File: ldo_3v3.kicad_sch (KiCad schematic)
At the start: 5 parts, among them U8 NCP1117-3.3

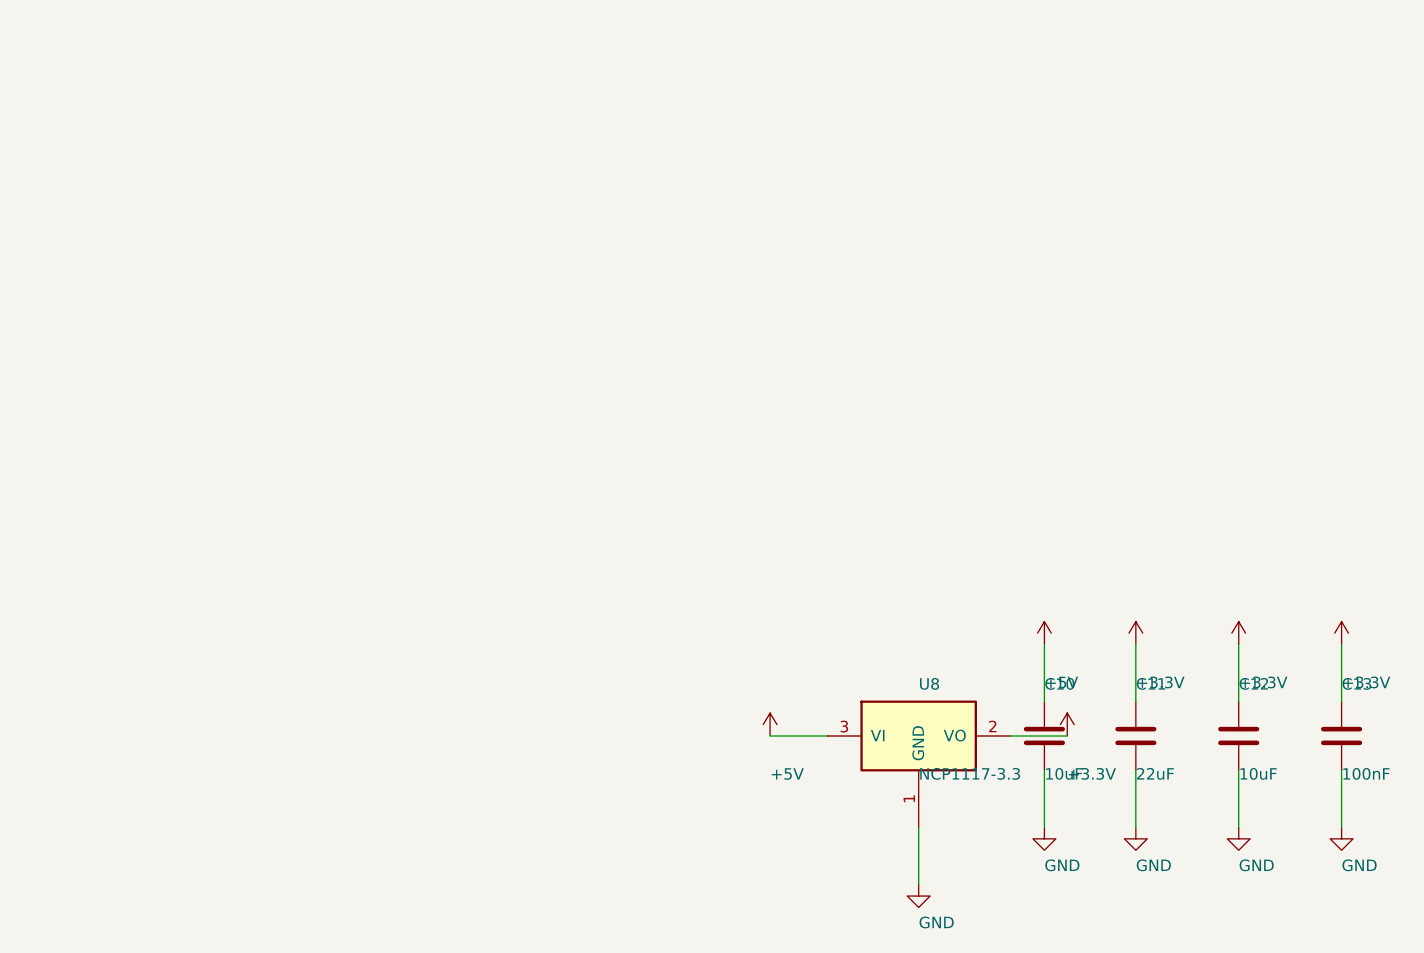
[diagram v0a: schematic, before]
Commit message: WIP: J18/Q2/Q3/R30/R31 + reguardado KiCad de todas las hojas
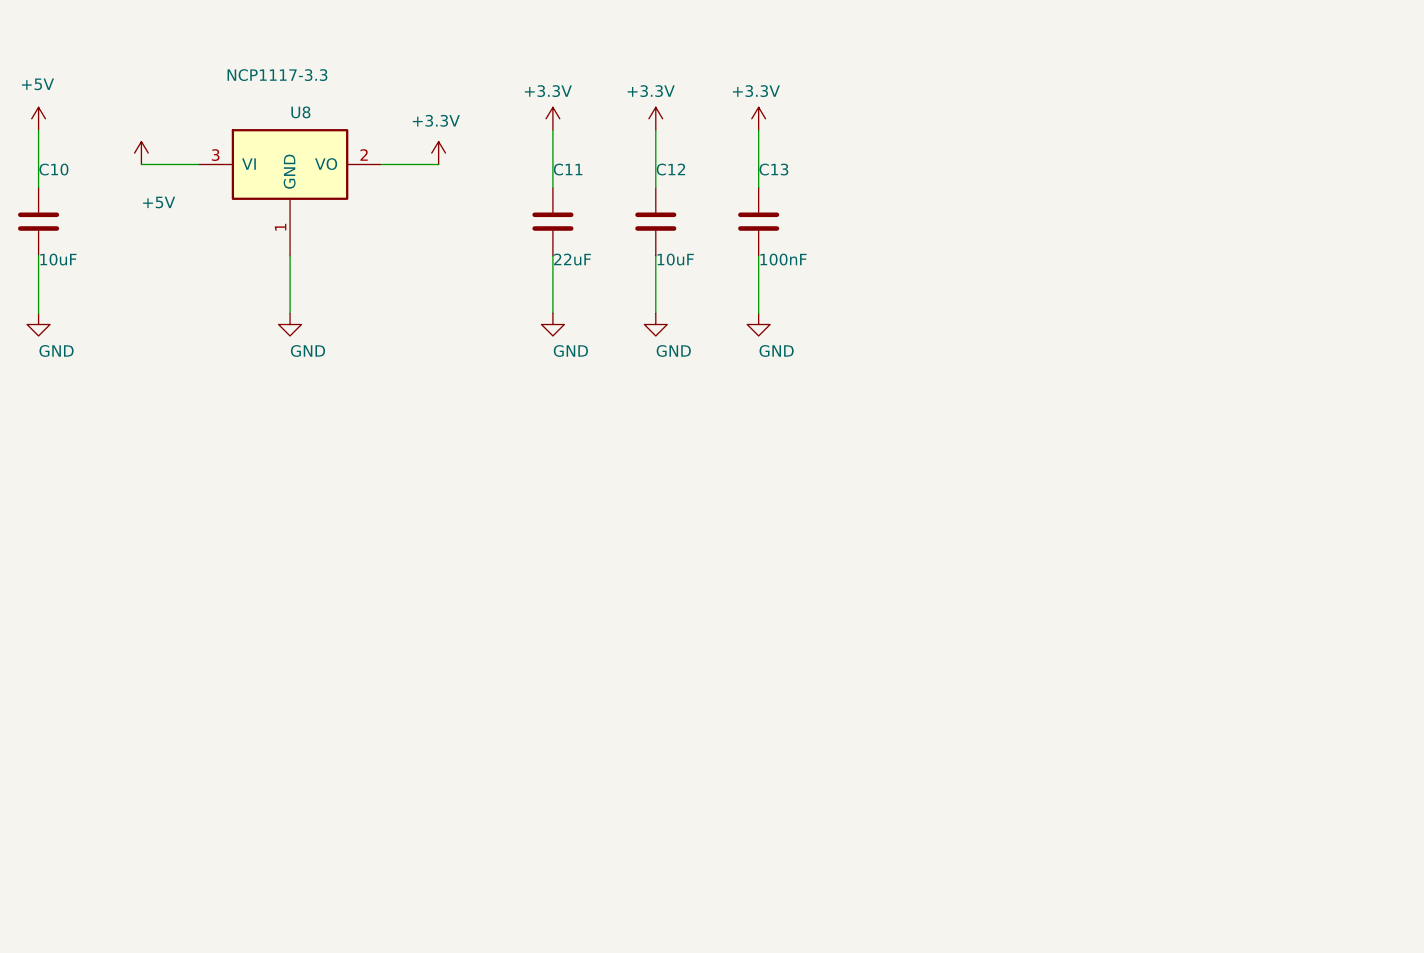
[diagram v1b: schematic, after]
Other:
- moved on the sheet: C10, C11, C12, C13, U8

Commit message: friday changes
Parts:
- C10, C12: DigiKey (none) -> 490-GRM21BR70J106KA73LTR-ND; MPN (none) -> GRM21BR70J106KA73L; Manufacturer (none) -> Murata Electronics
- C11: DigiKey (none) -> 587-5464-2-ND; MPN (none) -> LMK212BBJ226MG-T; Manufacturer (none) -> Taiyo Yuden
- C13: DigiKey (none) -> 1276-1003-2-ND; MPN (none) -> CL21B104KBCNNNC; Manufacturer (none) -> Samsung Electro-Mechanics
- U8: DigiKey (none) -> NCP1117ST33T3GOSTR-ND
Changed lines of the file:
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@@
+			)
+		)
+		(property "DigiKey" "NCP1117ST33T3GOSTR-ND"
+			(at 0 0 0)
+			(effects
+				(font
+					(size 1.27 1.27)
+				)
+				(hide yes)
 			)
 		)
@@
 			)
 		)
+		(property "Manufacturer" "Murata Electronics"
+			(at 0 0 0)
+			(effects
+				(font
+					(size 1.27 1.27)
+				)
+				(hide yes)
+			)
+		)
+		(property "MPN" "GRM21BR70J106KA73L"
+			(at 0 0 0)
+			(effects
+				(font
+					(size 1.27 1.27)
+				)
+				(hide yes)
+			)
+		)
+		(property "DigiKey" "490-GRM21BR70J106KA73LTR-ND"
+			(at 0 0 0)
+			(effects
+				(font
+					(size 1.27 1.27)
+				)
+				(hide yes)
+			)
+		)
 		(pin "1"
 		)
@@
 			)
 		)
+		(property "Manufacturer" "Taiyo Yuden"
+			(at 0 0 0)
+			(effects
+				(font
+					(size 1.27 1.27)
+				)
+				(hide yes)
+			)
+		)
+		(property "MPN" "LMK212BBJ226MG-T"
+			(at 0 0 0)
+			(effects
+				(font
+					(size 1.27 1.27)
+				)
+				(hide yes)
+			)
+		)
+		(property "DigiKey" "587-5464-2-ND"
+			(at 0 0 0)
+			(effects
+				(font
+					(size 1.27 1.27)
+				)
+				(hide yes)
+			)
+		)
 		(pin "1"
 		)
@@
 			)
 		)
+		(property "Manufacturer" "Murata Electronics"
+			(at 0 0 0)
+			(effects
+				(font
+					(size 1.27 1.27)
+				)
+				(hide yes)
+			)
+		)
+		(property "MPN" "GRM21BR70J106KA73L"
+			(at 0 0 0)
+			(effects
+				(font
+					(size 1.27 1.27)
+				)
+				(hide yes)
+			)
+		)
+		(property "DigiKey" "490-GRM21BR70J106KA73LTR-ND"
+			(at 0 0 0)
+			(effects
+				(font
+					(size 1.27 1.27)
+				)
+				(hide yes)
+			)
+		)
 		(pin "1"
 		)
@@
 				(hide yes)
 			)
+		)
+		(property "Manufacturer" "Samsung Electro-Mechanics"
+			(at 0 0 0)
+			(effects
+				(font
+					(size 1.27 1.27)
+				)
+				(hide yes)
+			)
+		)
+		(property "MPN" "CL21B104KBCNNNC"
+			(at 0 0 0)
+			(effects
+				(font
+					(size 1.27 1.27)
+				)
+				(hide yes)
+			)
+		)
+		(property "DigiKey" "1276-1003-2-ND"
+			(at 0 0 0)
+			(effects
+				(font
+					(size 1.27 1.27)
+				)
+				(hide yes)
+			)

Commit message: schematic updated
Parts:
- renumbered C10 to C37, C11 to C38, C12 to C39, C13 to C40, U8 to U9
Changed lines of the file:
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@@
 		(on_board yes)
 		(dnp no)
-		(property "Reference" "U8"
+		(property "Reference" "U9"
 			(at 123.19 77.55 0)
 			(effects
@@
 			(project "controlcarreta"
 				(path "/9232987b-e923-413e-abd9-77ced6cc4c47/20ed934b-5521-4cfc-8a1f-2c37d693b780"
-					(reference "U8")
+					(reference "U9")
 					(unit 1)
 				)
@@
 		(on_board yes)
 		(dnp no)
-		(property "Reference" "#PWR0505"
+		(property "Reference" "#PWR0163"
 			(at 106.68 77.55 0)
 			(effects
@@
 			(project "controlcarreta"
 				(path "/9232987b-e923-413e-abd9-77ced6cc4c47/20ed934b-5521-4cfc-8a1f-2c37d693b780"
-					(reference "#PWR0505")
+					(reference "#PWR0163")
 					(unit 1)
 				)
@@
 		(on_board yes)
 		(dnp no)
-		(property "Reference" "#PWR0506"
+		(property "Reference" "#PWR0165"
 			(at 139.7 77.55 0)
 			(effects
@@
 			(project "controlcarreta"
 				(path "/9232987b-e923-413e-abd9-77ced6cc4c47/20ed934b-5521-4cfc-8a1f-2c37d693b780"
-					(reference "#PWR0506")
+					(reference "#PWR0165")
 					(unit 1)
 				)
@@
 		(on_board yes)
 		(dnp no)
-		(property "Reference" "#PWR0507"
+		(property "Reference" "#PWR0164"
 			(at 123.19 94.06 0)
 			(effects
@@
 			(project "controlcarreta"
 				(path "/9232987b-e923-413e-abd9-77ced6cc4c47/20ed934b-5521-4cfc-8a1f-2c37d693b780"
-					(reference "#PWR0507")
+					(reference "#PWR0164")
 					(unit 1)
 				)
@@
 		(on_board yes)
 		(dnp no)
-		(property "Reference" "C10"
+		(property "Reference" "C37"
 			(at 95.25 83.9 0)
 			(effects
@@
 			(project "controlcarreta"
 				(path "/9232987b-e923-413e-abd9-77ced6cc4c47/20ed934b-5521-4cfc-8a1f-2c37d693b780"
-					(reference "C10")
+					(reference "C37")
 					(unit 1)
 				)
@@
 		(on_board yes)
 		(dnp no)
-		(property "Reference" "#PWR0508"
+		(property "Reference" "#PWR0161"
 			(at 95.25 73.74 0)
 			(effects
@@
 			(project "controlcarreta"
 				(path "/9232987b-e923-413e-abd9-77ced6cc4c47/20ed934b-5521-4cfc-8a1f-2c37d693b780"
-					(reference "#PWR0508")
+					(reference "#PWR0161")
 					(unit 1)
 				)
@@
 		(on_board yes)
 		(dnp no)
-		(property "Reference" "#PWR0509"
+		(property "Reference" "#PWR0162"
 			(at 95.25 94.06 0)
 			(effects
@@
 			(project "controlcarreta"
 				(path "/9232987b-e923-413e-abd9-77ced6cc4c47/20ed934b-5521-4cfc-8a1f-2c37d693b780"
-					(reference "#PWR0509")
+					(reference "#PWR0162")
 					(unit 1)
 				)
@@
 		(on_board yes)
 		(dnp no)
-		(property "Reference" "C11"
+		(property "Reference" "C38"
 			(at 152.4 83.9 0)
 			(effects
@@
 			(project "controlcarreta"
 				(path "/9232987b-e923-413e-abd9-77ced6cc4c47/20ed934b-5521-4cfc-8a1f-2c37d693b780"
-					(reference "C11")
+					(reference "C38")
 					(unit 1)
 				)
@@
 		(on_board yes)
 		(dnp no)
-		(property "Reference" "#PWR0510"
+		(property "Reference" "#PWR0166"
 			(at 152.4 73.74 0)
 			(effects
@@
 			(project "controlcarreta"
 				(path "/9232987b-e923-413e-abd9-77ced6cc4c47/20ed934b-5521-4cfc-8a1f-2c37d693b780"
-					(reference "#PWR0510")
+					(reference "#PWR0166")
 					(unit 1)
 				)
@@
 		(on_board yes)
 		(dnp no)
-		(property "Reference" "#PWR0511"
+		(property "Reference" "#PWR0167"
 			(at 152.4 94.06 0)
 			(effects
@@
 			(project "controlcarreta"
 				(path "/9232987b-e923-413e-abd9-77ced6cc4c47/20ed934b-5521-4cfc-8a1f-2c37d693b780"
-					(reference "#PWR0511")
+					(reference "#PWR0167")
 					(unit 1)
 				)
@@
 		(on_board yes)
 		(dnp no)
-		(property "Reference" "C12"
+		(property "Reference" "C39"
 			(at 163.83 83.9 0)
 			(effects
@@
 			(project "controlcarreta"
 				(path "/9232987b-e923-413e-abd9-77ced6cc4c47/20ed934b-5521-4cfc-8a1f-2c37d693b780"
-					(reference "C12")
+					(reference "C39")
 					(unit 1)
 				)
@@
 		(on_board yes)
 		(dnp no)
-		(property "Reference" "#PWR0512"
+		(property "Reference" "#PWR0168"
 			(at 163.83 73.74 0)
 			(effects
@@
 			(project "controlcarreta"
 				(path "/9232987b-e923-413e-abd9-77ced6cc4c47/20ed934b-5521-4cfc-8a1f-2c37d693b780"
-					(reference "#PWR0512")
+					(reference "#PWR0168")
 					(unit 1)
 				)
@@
 		(on_board yes)
 		(dnp no)
-		(property "Reference" "#PWR0513"
+		(property "Reference" "#PWR0169"
 			(at 163.83 94.06 0)
 			(effects
@@
 			(project "controlcarreta"
 				(path "/9232987b-e923-413e-abd9-77ced6cc4c47/20ed934b-5521-4cfc-8a1f-2c37d693b780"
-					(reference "#PWR0513")
+					(reference "#PWR0169")
 					(unit 1)
 				)
@@
 		(on_board yes)
 		(dnp no)
-		(property "Reference" "C13"
+		(property "Reference" "C40"
 			(at 175.26 83.9 0)
 			(effects
@@
 			(project "controlcarreta"
 				(path "/9232987b-e923-413e-abd9-77ced6cc4c47/20ed934b-5521-4cfc-8a1f-2c37d693b780"
-					(reference "C13")
+					(reference "C40")
 					(unit 1)
 				)
@@
 		(on_board yes)
 		(dnp no)
-		(property "Reference" "#PWR0514"
+		(property "Reference" "#PWR0170"
 			(at 175.26 73.74 0)
 			(effects
@@
 			(project "controlcarreta"
 				(path "/9232987b-e923-413e-abd9-77ced6cc4c47/20ed934b-5521-4cfc-8a1f-2c37d693b780"
-					(reference "#PWR0514")
+					(reference "#PWR0170")
 					(unit 1)
 				)
@@
 		(on_board yes)
 		(dnp no)
-		(property "Reference" "#PWR0515"
+		(property "Reference" "#PWR0171"
 			(at 175.26 94.06 0)
 			(effects
@@
 			(project "controlcarreta"
 				(path "/9232987b-e923-413e-abd9-77ced6cc4c47/20ed934b-5521-4cfc-8a1f-2c37d693b780"
-					(reference "#PWR0515")
-					(unit 1)
-				)
+					(reference "#PWR0171")
+					(unit 1)
+				)

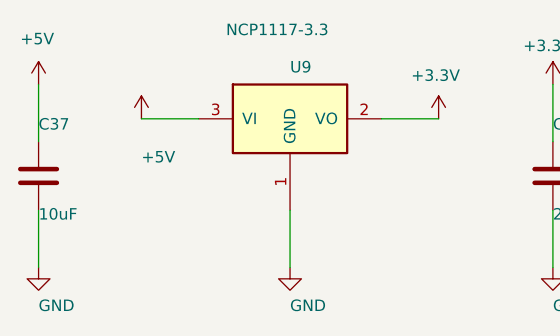
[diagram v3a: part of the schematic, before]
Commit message: removed gps headear
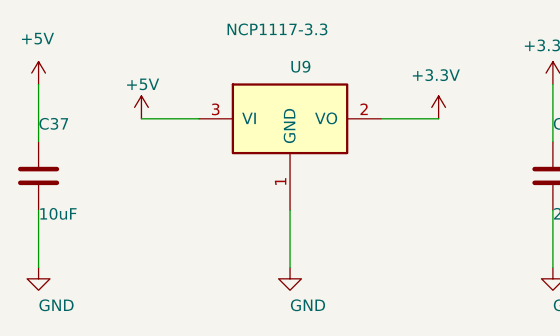
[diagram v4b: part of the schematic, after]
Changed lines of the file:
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@@
 		)
 		(property "Value" "+5V"
-			(at 106.68 87.55 0)
+			(at 104.902 79.502 0)
 			(effects
 				(font

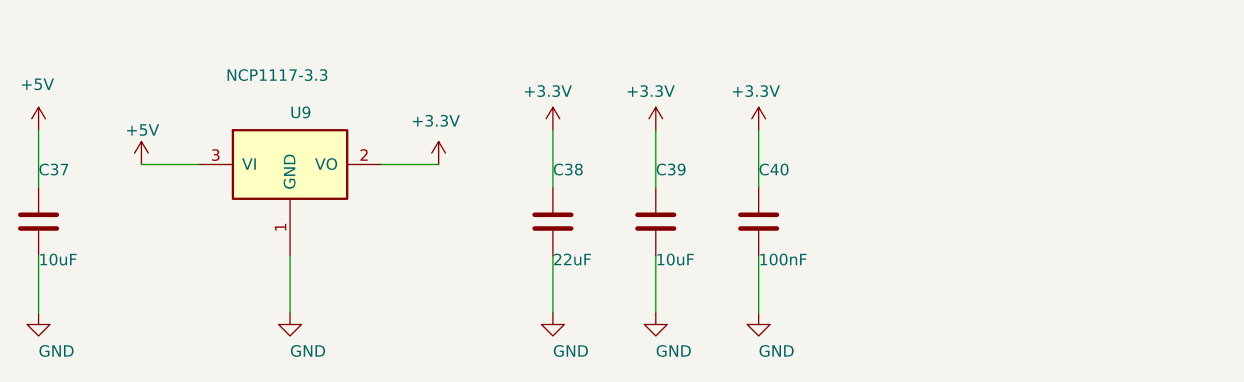
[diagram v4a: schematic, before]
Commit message: 2 power source
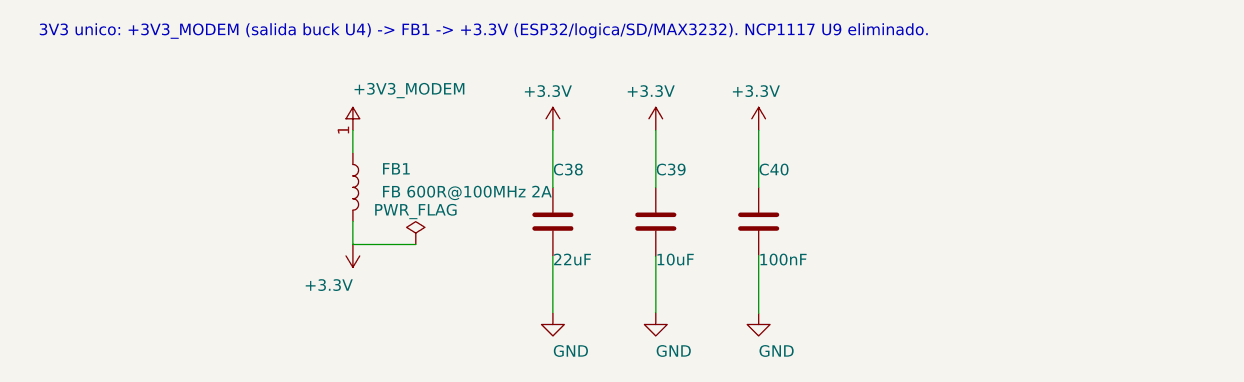
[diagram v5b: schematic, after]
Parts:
- removed C37: 10uF, Capacitor_SMD:C_0805_2012Metric_Pad1.18x1.45mm_HandSolder, symbol Device:C
- removed U9: NCP1117-3.3, Package_TO_SOT_SMD:SOT-223-3_TabPin2, symbol controlcarreta:NCP1117-3.3_SOT223
- added FB1: FB 600R@100MHz 2A, Inductor_SMD:L_0805_2012Metric, symbol Device:L
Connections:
- net +3.3V: now also FB1.2
- new net +3V3_MODEM: FB1.1
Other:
- note added: "3V3 unico: +3V3_MODEM (salida buck U4) -> FB1 -> +3.3V (ESP32/logica/SD/MAX3232). NCP1117 U9 eliminado."
- title: LDO 3V3 - Regulador lineal NCP1117-3.3 y desacoplo -> FILTRO 3V3 - Ferrita + bulk (ESP32/logica); 3V3 unico desde buck U4

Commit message: last changes in work
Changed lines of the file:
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@@
 				)
 				(justify left bottom)
+				(hide yes)
 			)
 		)
